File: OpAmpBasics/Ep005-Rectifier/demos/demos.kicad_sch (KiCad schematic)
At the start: 32 parts, among them J1 Conn_01x02_Socket, J2 Conn_01x02_Socket, J3 Conn_01x02_Socket, J4 Conn_01x02_Socket, J5 Conn_01x02_Socket, J6 Conn_01x02_Socket, J7 Conn_01x02_Socket, J8 Conn_01x02_Socket, U1 TL072, U2 TL072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

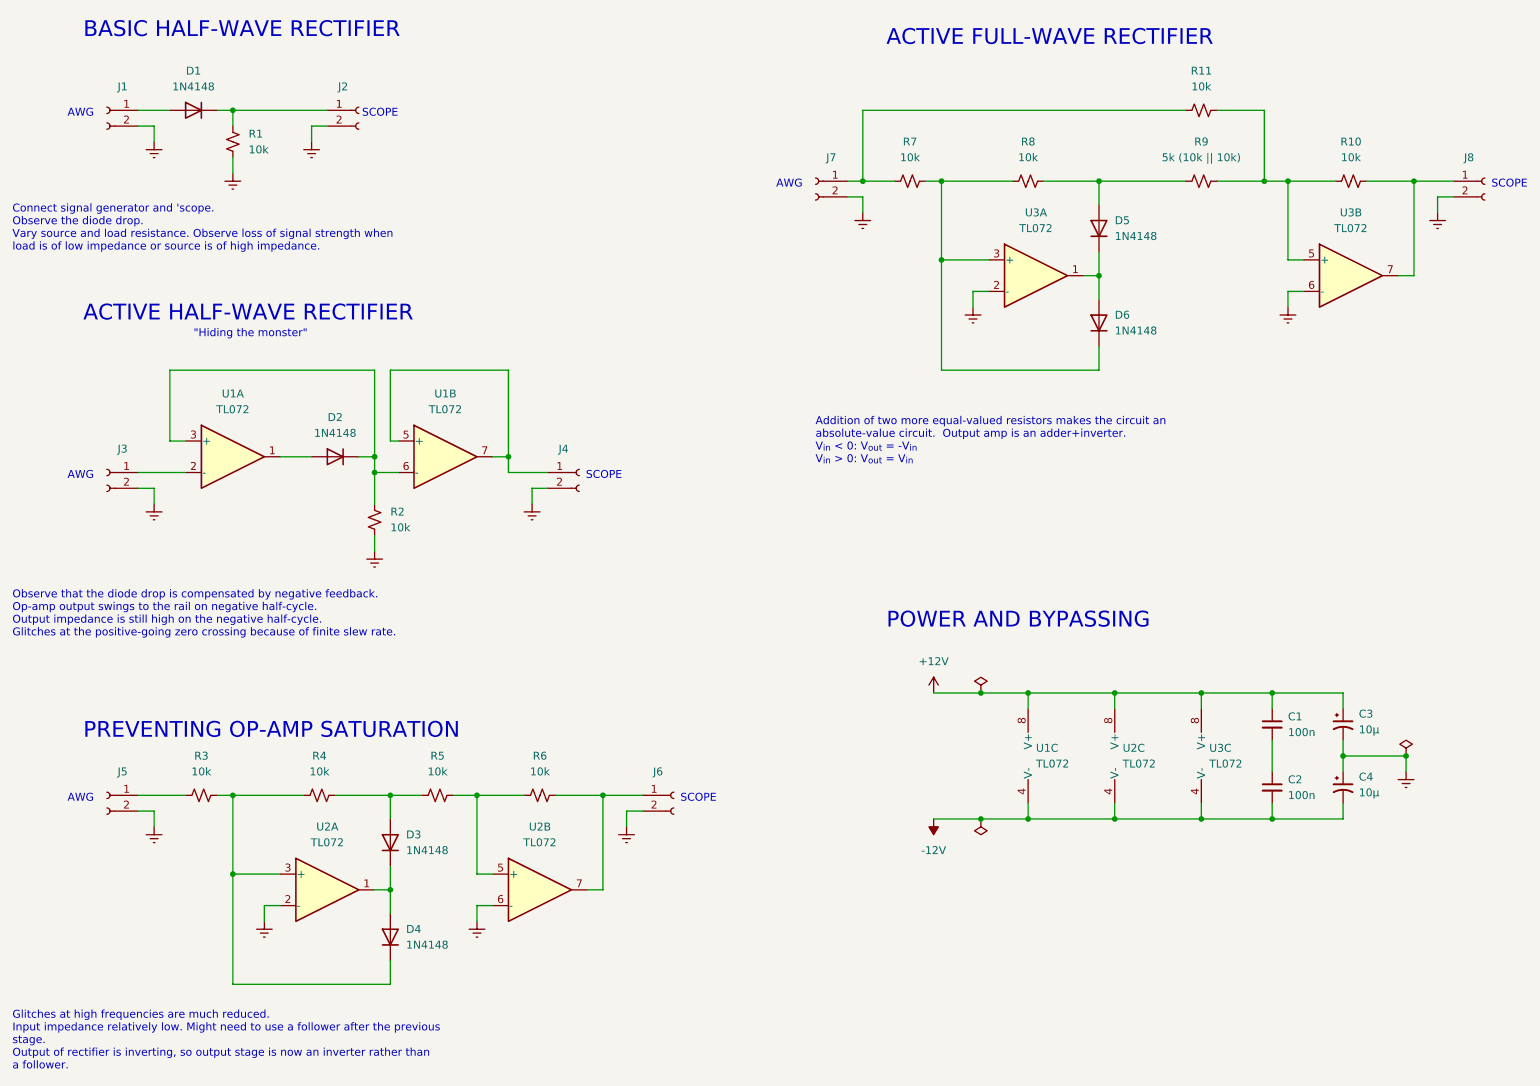
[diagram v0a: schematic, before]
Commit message: Put the opamps with (-) on top.
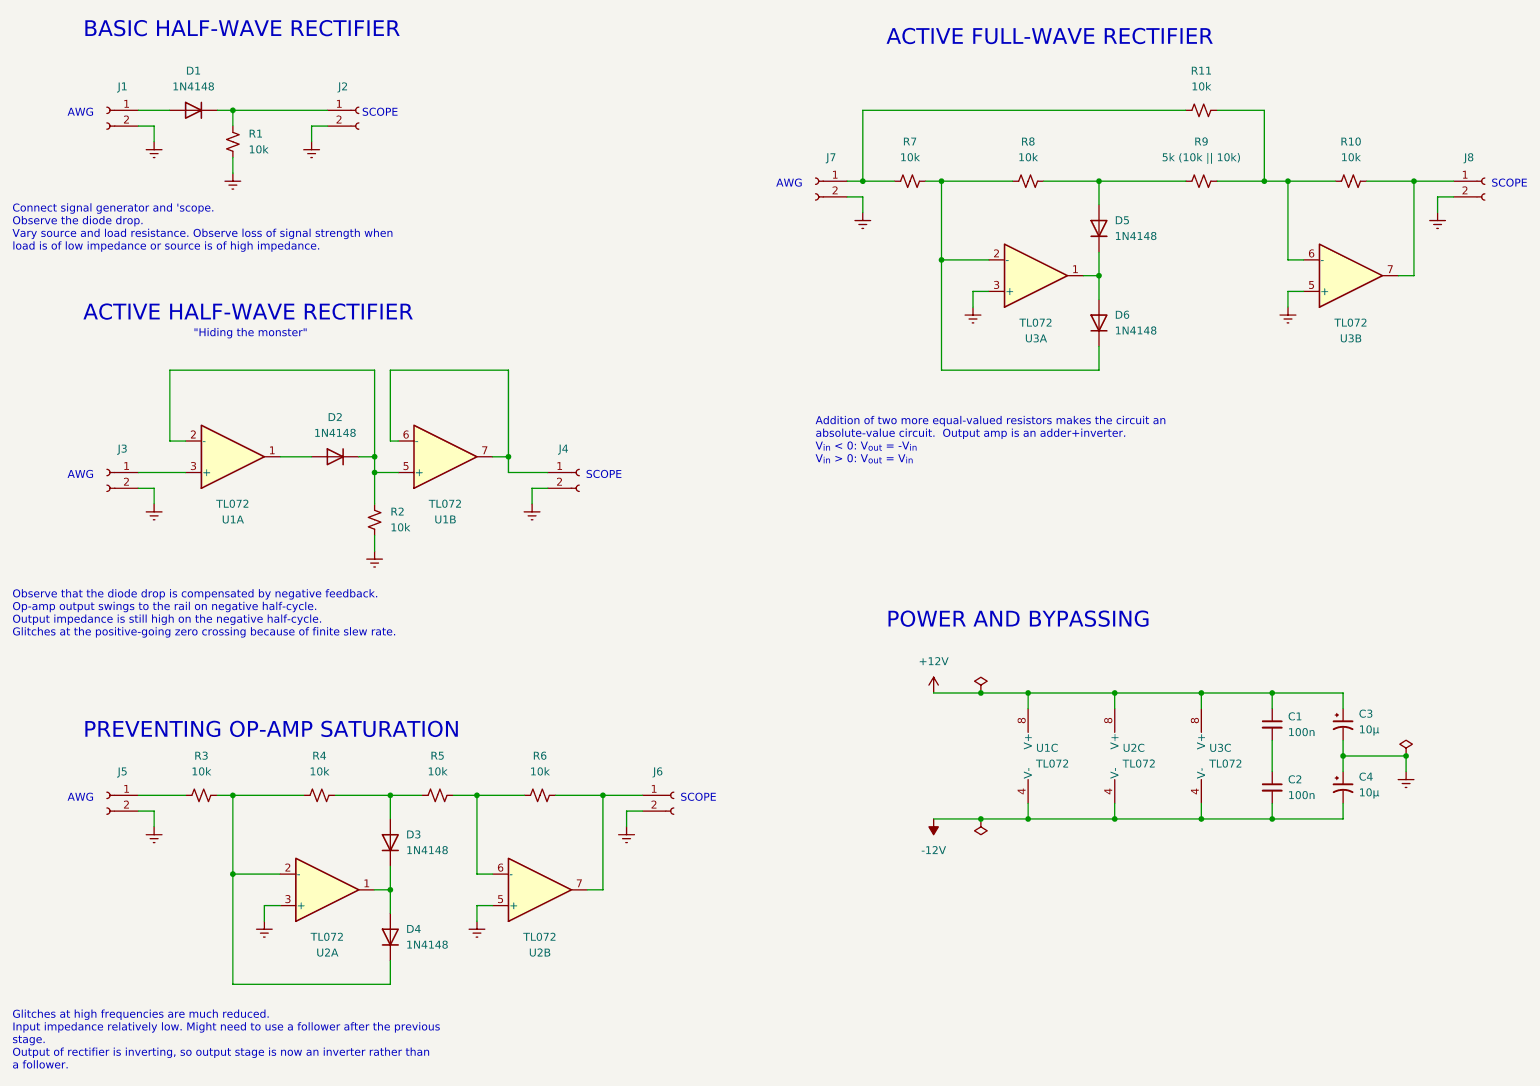
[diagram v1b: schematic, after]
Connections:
- net Earth: now also U2.3 (+), U2.5 (+), U3.3 (+), U3.5 (+); no longer U2.2 (-), U2.6 (-), U3.2 (-), U3.6 (-)
- net at R10.1, R11.2, R9.2: now also U3.6 (-); no longer U3.5 (+)
- net at R5.2, R6.1: now also U2.6 (-); no longer U2.5 (+)
- net at U1.2 (-): now also D2.1 (K), R2.1, U1.5 (+); no longer J3.1 (Pin_1)
- net at D4.1 (K), R3.2, R4.1: now also U2.2 (-); no longer U2.3 (+)
- net at D6.1 (K), R7.2, R8.1: now also U3.2 (-); no longer U3.3 (+)
- net at J4.1 (Pin_1), U1.7: now also U1.6 (-); no longer U1.5 (+)
- new net: J3.1 (Pin_1), U1.3 (+)
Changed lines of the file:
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@@
     )
   )
-  (symbol (lib_id "Amplifier_Operational:TL072") (at 55.88 92.71 0) (unit 1)
-    (in_bom yes) (on_board yes) (dnp no) (fields_autoplaced)
-    (property "Reference" "U1" (at 55.88 82.55 0)
-      (effects (font (size 1.27 1.27)))
-    )
-    (property "Value" "TL072" (at 55.88 85.09 0)
+  (symbol (lib_id "Amplifier_Operational:TL072") (at 55.88 92.71 0) (mirror x) (unit 1)
+    (in_bom yes) (on_board yes) (dnp no)
+    (property "Reference" "U1" (at 55.88 102.87 0)
+      (effects (font (size 1.27 1.27)))
+    )
+    (property "Value" "TL072" (at 55.88 100.33 0)
       (effects (font (size 1.27 1.27)))
     )
@@
     )
   )
-  (symbol (lib_id "Amplifier_Operational:TL072") (at 90.17 92.71 0) (unit 2)
-    (in_bom yes) (on_board yes) (dnp no) (fields_autoplaced)
-    (property "Reference" "U1" (at 90.17 82.55 0)
-      (effects (font (size 1.27 1.27)))
-    )
-    (property "Value" "TL072" (at 90.17 85.09 0)
+  (symbol (lib_id "Amplifier_Operational:TL072") (at 90.17 92.71 0) (mirror x) (unit 2)
+    (in_bom yes) (on_board yes) (dnp no)
+    (property "Reference" "U1" (at 90.17 102.87 0)
+      (effects (font (size 1.27 1.27)))
+    )
+    (property "Value" "TL072" (at 90.17 100.33 0)
       (effects (font (size 1.27 1.27)))
     )
@@
     )
   )
-  (symbol (lib_id "Amplifier_Operational:TL072") (at 105.41 162.56 0) (unit 2)
-    (in_bom yes) (on_board yes) (dnp no) (fields_autoplaced)
-    (property "Reference" "U2" (at 105.41 152.4 0)
-      (effects (font (size 1.27 1.27)))
-    )
-    (property "Value" "TL072" (at 105.41 154.94 0)
+  (symbol (lib_id "Amplifier_Operational:TL072") (at 105.41 162.56 0) (mirror x) (unit 2)
+    (in_bom yes) (on_board yes) (dnp no)
+    (property "Reference" "U2" (at 105.41 172.72 0)
+      (effects (font (size 1.27 1.27)))
+    )
+    (property "Value" "TL072" (at 105.41 170.18 0)
       (effects (font (size 1.27 1.27)))
     )
@@
     )
   )
-  (symbol (lib_id "Amplifier_Operational:TL072") (at 236.22 63.5 0) (unit 2)
-    (in_bom yes) (on_board yes) (dnp no) (fields_autoplaced)
-    (property "Reference" "U3" (at 236.22 53.34 0)
-      (effects (font (size 1.27 1.27)))
-    )
-    (property "Value" "TL072" (at 236.22 55.88 0)
+  (symbol (lib_id "Amplifier_Operational:TL072") (at 236.22 63.5 0) (mirror x) (unit 2)
+    (in_bom yes) (on_board yes) (dnp no)
+    (property "Reference" "U3" (at 236.22 73.66 0)
+      (effects (font (size 1.27 1.27)))
+    )
+    (property "Value" "TL072" (at 236.22 71.12 0)
       (effects (font (size 1.27 1.27)))
     )
@@
     )
   )
-  (symbol (lib_id "Amplifier_Operational:TL072") (at 71.12 162.56 0) (unit 1)
-    (in_bom yes) (on_board yes) (dnp no) (fields_autoplaced)
-    (property "Reference" "U2" (at 71.12 152.4 0)
-      (effects (font (size 1.27 1.27)))
-    )
-    (property "Value" "TL072" (at 71.12 154.94 0)
+  (symbol (lib_id "Amplifier_Operational:TL072") (at 71.12 162.56 0) (mirror x) (unit 1)
+    (in_bom yes) (on_board yes) (dnp no)
+    (property "Reference" "U2" (at 71.12 172.72 0)
+      (effects (font (size 1.27 1.27)))
+    )
+    (property "Value" "TL072" (at 71.12 170.18 0)
       (effects (font (size 1.27 1.27)))
     )
@@
     )
   )
-  (symbol (lib_id "Amplifier_Operational:TL072") (at 185.42 63.5 0) (unit 1)
-    (in_bom yes) (on_board yes) (dnp no) (fields_autoplaced)
-    (property "Reference" "U3" (at 185.42 53.34 0)
-      (effects (font (size 1.27 1.27)))
-    )
-    (property "Value" "TL072" (at 185.42 55.88 0)
-      (effects (font (size 1.27 1.27)))
-    )
+  (symbol (lib_id "Amplifier_Operational:TL072") (at 185.42 63.5 0) (mirror x) (unit 1)
+    (in_bom yes) (on_board yes) (dnp no)
+    (property "Reference" "U3" (at 185.42 73.66 0)
+      (effects (font (size 1.27 1.27)))
+    )
+    (property "Value" "TL072" (at 185.42 71.12 0)
+      (effects (font (size 1.27 1.27)))
+    )
